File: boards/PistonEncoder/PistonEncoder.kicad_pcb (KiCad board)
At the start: 2 copper layers, 26 parts, among them J1 ISP, J2 PedalExt, J3 LED_Pwr, J4 LEDs1, J5 LEDs2, J6 Pistons1, J7 Pistons2, J8 BoardCon, U1 ATmega48-20P, U2 ULN2803A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

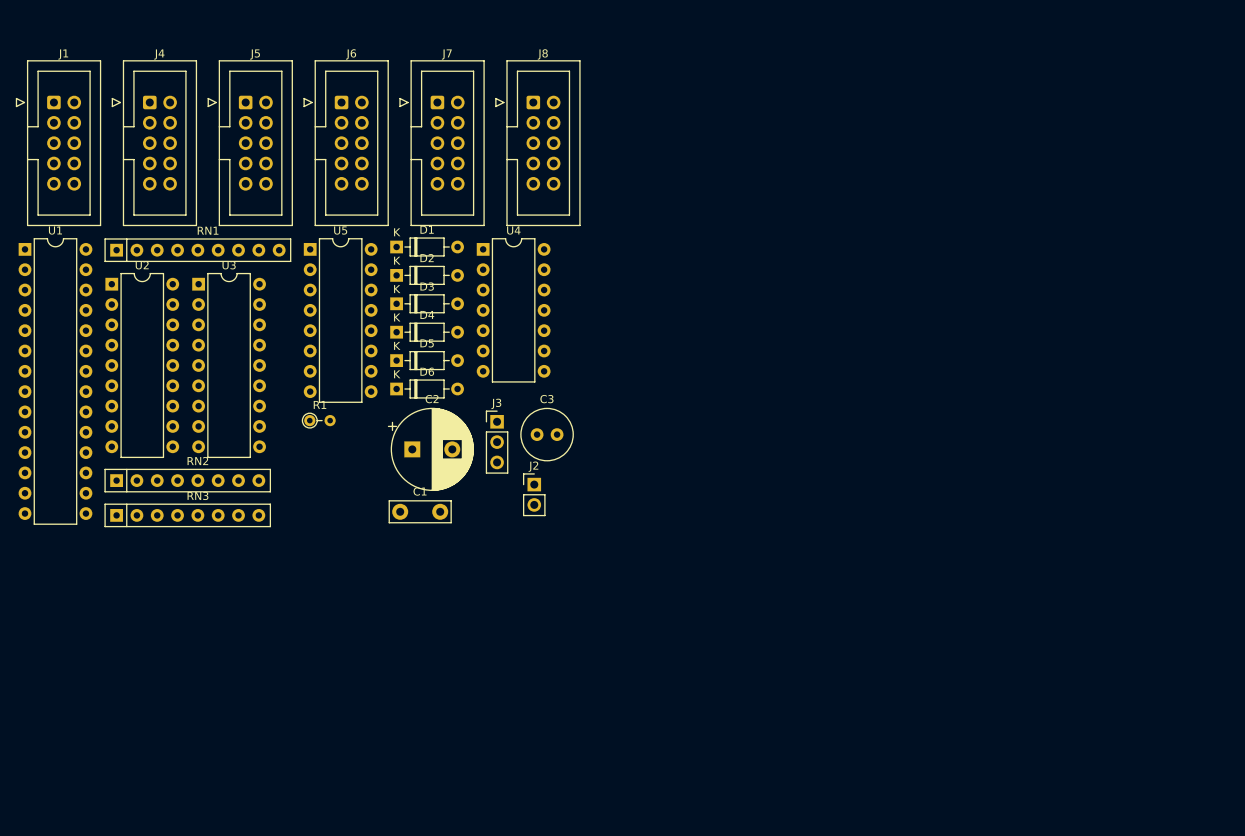
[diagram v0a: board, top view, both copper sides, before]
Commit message: PCB layout for keyboard scanner and piston encoder
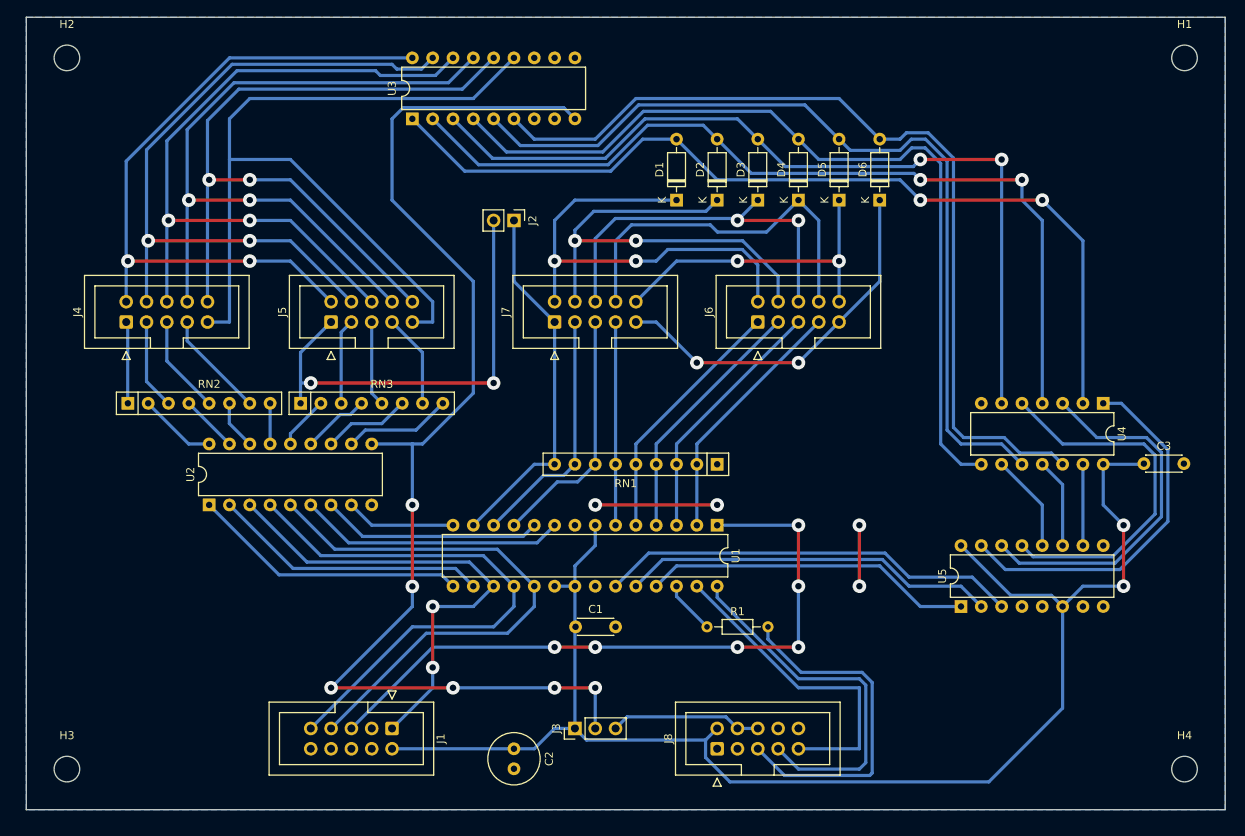
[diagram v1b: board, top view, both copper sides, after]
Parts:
- added H1: MountingHole, MountingHole:MountingHole_3.2mm_M3, F.Cu at (210.8, 50.8)
- added H2: MountingHole, MountingHole:MountingHole_3.2mm_M3, F.Cu at (71.1, 50.8)
- added H3: MountingHole, MountingHole:MountingHole_3.2mm_M3, F.Cu at (71.1, 139.7)
- added H4: MountingHole, MountingHole:MountingHole_3.2mm_M3, F.Cu at (210.8, 139.7)
- C1: value 100nF -> C; footprint Capacitor_THT:C_Disc_D7.5mm_W2.5mm_P5.00mm -> Capacitor_THT:C_Disc_D4.3mm_W1.9mm_P5.00mm
- C2: footprint Capacitor_THT:CP_Radial_D10.0mm_P5.00mm -> Capacitor_THT:C_Radial_D6.3mm_H7.0mm_P2.50mm
- C3: value 100nF -> C; footprint Capacitor_THT:C_Radial_D6.3mm_H11.0mm_P2.50mm -> Capacitor_THT:C_Disc_D4.3mm_W1.9mm_P5.00mm
- J2: value PedalExt -> Ext
- J3: value LED_Pwr -> PWR
- J4: value LEDs1 -> LED1
- J5: value LEDs2 -> LED2
- R1: value 220 -> R; footprint Resistor_THT:R_Axial_DIN0204_L3.6mm_D1.6mm_P2.54mm_Vertical -> Resistor_THT:R_Axial_DIN0204_L3.6mm_D1.6mm_P7.62mm_Horizontal
- RN2, RN3: value R_Pack04 -> R_Pack04_SIP_Split
- moved U1 93.1 mm to (152.4, 109.2), turned to -90 degrees
- moved U5 92.8 mm to (182.9, 119.4), turned to 90 degrees
- moved J1 88.9 mm to (111.8, 134.6), turned to -90 degrees
- moved J8 84.0 mm to (152.4, 137.2), turned to 90 degrees
- moved U4 79.9 mm to (200.7, 94.0), turned to -90 degrees
- moved RN1 79.7 mm to (152.4, 101.6), turned to 180 degrees
- moved C3 75.9 mm to (205.7, 101.5)
- moved D6 64.8 mm to (172.7, 68.6), turned to 90 degrees
- moved D5 58.8 mm to (167.6, 68.6), turned to 90 degrees
- moved J6 58.8 mm to (157.5, 83.8), turned to 90 degrees
- moved R1 55.9 mm to (151.1, 121.9)
- moved D4 52.9 mm to (162.6, 68.6), turned to 90 degrees
- moved D3 47.0 mm to (157.5, 68.6), turned to 90 degrees
- moved D2 41.2 mm to (152.4, 68.6), turned to 90 degrees
- moved J3 39.5 mm to (134.6, 134.6), turned to 90 degrees
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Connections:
- J2 pad 1: Net-(J2-Pin_1) -> P8
- J6 pad 1: Net-(J6-Pin_1) -> P4
- J6 pad 3: Net-(J6-Pin_3) -> P3
- J6 pad 5: Net-(J6-Pin_5) -> P2
- J6 pad 7: Net-(J6-Pin_7) -> P1
- J7 pad 1: Net-(J2-Pin_1) -> P8
- J7 pad 3: Net-(J7-Pin_3) -> P7
- J7 pad 5: Net-(J7-Pin_5) -> P6
- J7 pad 7: Net-(J7-Pin_7) -> P5
- RN1 pad 2: Net-(J6-Pin_1) -> P1
- RN1 pad 3: Net-(J6-Pin_3) -> P2
- RN1 pad 4: Net-(J6-Pin_5) -> P3
- RN1 pad 5: Net-(J6-Pin_7) -> P4
- RN1 pad 6: Net-(J2-Pin_1) -> P5
- RN1 pad 7: Net-(J7-Pin_3) -> P6
- RN1 pad 8: Net-(J7-Pin_5) -> P7
- RN1 pad 9: Net-(J7-Pin_7) -> P8
- RN2 pad 1: Net-(J4-Pin_7) -> Net-(J4-Pin_1)
- RN2 pad 2: Net-(J4-Pin_5) -> Net-(RN2A-R1.2)
- RN2 pad 4: Net-(J4-Pin_1) -> Net-(RN2B-R2.2)
- RN2 pad 5: Net-(RN2-R4.2) -> Net-(J4-Pin_5)
- RN2 pad 6: Net-(RN2-R3.2) -> Net-(RN2C-R3.2)
- RN2 pad 7: Net-(RN2-R2.2) -> Net-(J4-Pin_7)
- RN3 pad 1: Net-(J5-Pin_7) -> Net-(J2-Pin_2)
- RN3 pad 2: Net-(J5-Pin_5) -> Net-(RN3A-R1.2)
- RN3 pad 4: Net-(J2-Pin_2) -> Net-(RN3B-R2.2)
- RN3 pad 5: Net-(RN3-R4.2) -> Net-(J5-Pin_5)
- RN3 pad 6: Net-(RN3-R3.2) -> Net-(RN3C-R3.2)
- RN3 pad 7: Net-(RN3-R2.2) -> Net-(J5-Pin_7)
- U1 pad 11: Net-(J7-Pin_3) -> P6
- U1 pad 12: Net-(J7-Pin_5) -> P7
- U1 pad 13: Net-(J7-Pin_7) -> P8
- U1 pad 2: Net-(J6-Pin_1) -> P1
- U1 pad 23: A1 -> A3
- U1 pad 25: A3 -> A1
- U1 pad 3: Net-(J6-Pin_3) -> P2
- U1 pad 4: Net-(J6-Pin_5) -> P3
- U1 pad 5: Net-(J6-Pin_7) -> P4
- U1 pad 6: Net-(J2-Pin_1) -> P5
- U2 pad 1: Net-(U1-PB0) -> Net-(U1-PB1)
- U2 pad 12: Net-(RN3-R2.2) -> Net-(RN3C-R3.2)
- U2 pad 13: Net-(RN3-R3.2) -> Net-(RN3B-R2.2)
- U2 pad 14: Net-(RN3-R4.2) -> Net-(RN3A-R1.2)
- U2 pad 16: Net-(RN2-R2.2) -> Net-(RN2C-R3.2)
- U2 pad 17: Net-(RN2-R3.2) -> Net-(RN2B-R2.2)
- U2 pad 18: Net-(RN2-R4.2) -> Net-(RN2A-R1.2)
- U2 pad 2: Net-(U1-PB1) -> Net-(U1-PB2)
- U2 pad 3: Net-(U1-PB2) -> MOSI
- U2 pad 4: MOSI -> MISO
- U2 pad 5: MISO -> SCK
- U2 pad 6: SCK -> Net-(U1-XTAL1/PB6)
- U2 pad 7: Net-(U1-XTAL1/PB6) -> Net-(U1-XTAL2/PB7)
- U2 pad 8: Net-(U1-XTAL2/PB7) -> Net-(U1-PB0)
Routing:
- net +5V: track 0.00 -> 182.3 mm, vias 0 -> 2
- net Net-(J3-Pin_2): track 0.00 -> 150.6 mm, vias 0 -> 6
- net L1: track 0.00 -> 113.8 mm, vias 0 -> 2
- net L6: track 0.00 -> 111.1 mm
- net L2: track 0.00 -> 109.9 mm, vias 0 -> 2
- net L5: track 0.00 -> 109.0 mm
- net L4: track 0.00 -> 107.3 mm
- net L3: track 0.00 -> 106.0 mm, vias 0 -> 2
- net Net-(J4-Pin_9): track 0.00 -> 104.7 mm
- net Net-(J4-Pin_10): track 0.00 -> 93.6 mm, vias 0 -> 2
- net Net-(J4-Pin_8): track 0.00 -> 91.9 mm, vias 0 -> 2
- net Net-(J4-Pin_6): track 0.00 -> 90.5 mm, vias 0 -> 2
- net Net-(J4-Pin_4): track 0.00 -> 88.8 mm, vias 0 -> 2
- net Net-(J4-Pin_2): track 0.00 -> 86.4 mm, vias 0 -> 2
- net Reset: track 0.00 -> 85.5 mm, vias 0 -> 6
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- added copper zone on B.Cu, net GND
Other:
- board outline added: 149.9 x 99.1 mm

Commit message: Updated to KiCAD 8, fixed optocouplers for MIDI and added powersupplies
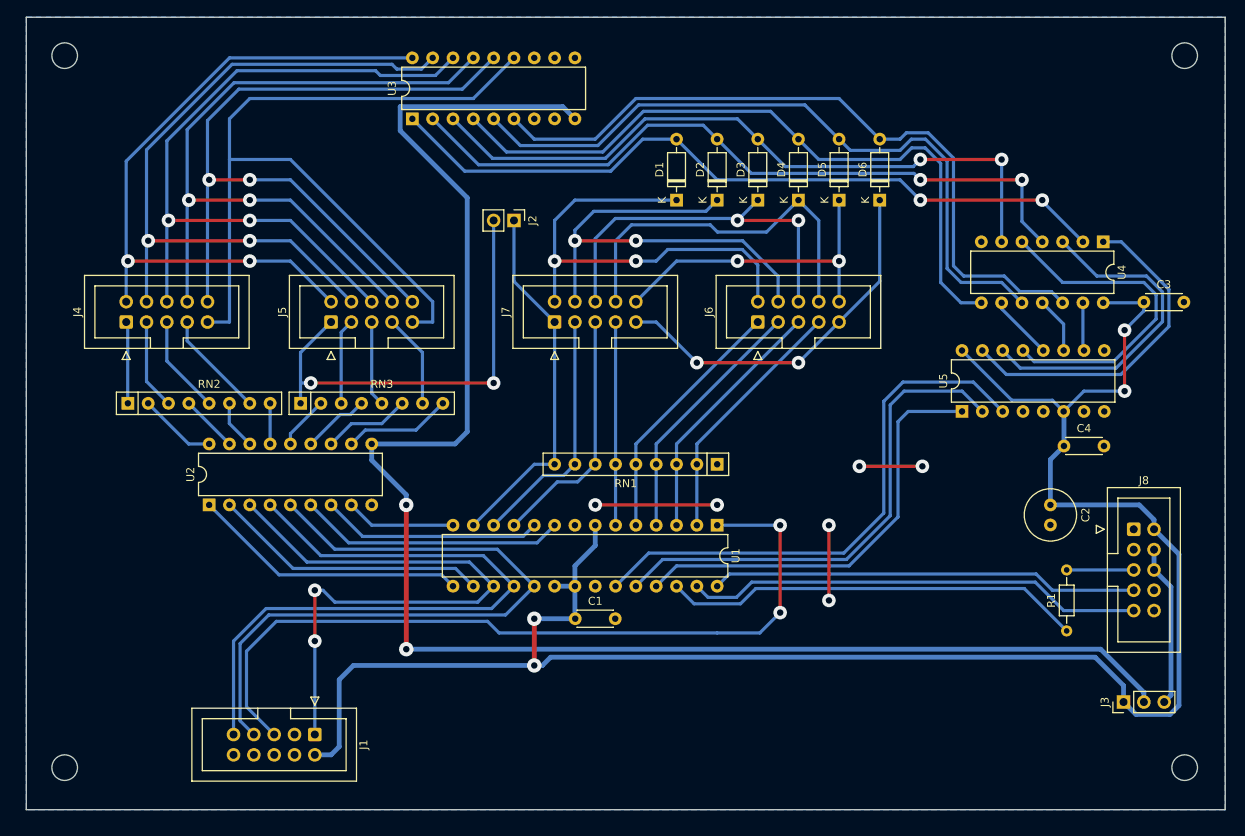
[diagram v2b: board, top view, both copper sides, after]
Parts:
- added C4: 100nF, Capacitor_THT:C_Disc_D4.3mm_W1.9mm_P5.00mm, F.Cu at (195.8, 99.3)
- C1, C3: value C -> 100nF
- C2: value C_Polarized -> 10uF
- moved C2 73.7 mm to (194.1, 106.7)
- moved J3 68.7 mm to (203.2, 131.3)
- moved J8 58.9 mm to (204.5, 109.7), turned to 0 degrees
- moved R1 45.0 mm to (196.1, 122.4), turned to 90 degrees
- moved U5 24.4 mm to (183.0, 95.0)
- moved C3 20.2 mm to (205.7, 81.3)
- moved U4 20.2 mm to (200.7, 73.8)
- moved J1 9.68 mm to (102.1, 135.4)
- moved C1 1.02 mm to (134.7, 120.9)
- moved H2 0.40 mm to (70.8, 50.5)
- moved H3 0.33 mm to (70.8, 139.5)
- moved H1 0.28 mm to (210.8, 50.5)
- moved H4 0.18 mm to (210.8, 139.5)
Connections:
- net Net-(J3-Pin_2) renamed /LED_PWR
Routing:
- net +5V: track 182.3 -> 241.3 mm, vias 2 -> 4
- net /LED_PWR: track 150.6 -> 202.2 mm, vias 6 -> 2
- net Interrupt: track 6.66 -> 52.7 mm
- net Net-(J8-Pin_5): track 43.9 -> 8.38 mm
- net L5: track 109.0 -> 88.8 mm
- net L4: track 107.3 -> 87.1 mm
- net L3: track 106.0 -> 85.8 mm
- net L1: track 113.8 -> 93.6 mm
- net L6: track 111.1 -> 90.9 mm
- net L2: track 109.9 -> 89.7 mm
- net SCK: track 68.9 -> 86.5 mm
- net SDA: track 40.8 -> 57.5 mm
- net A3: track 52.7 -> 68.7 mm
- net MOSI: track 60.7 -> 76.5 mm
- net A2: track 47.0 -> 62.6 mm
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
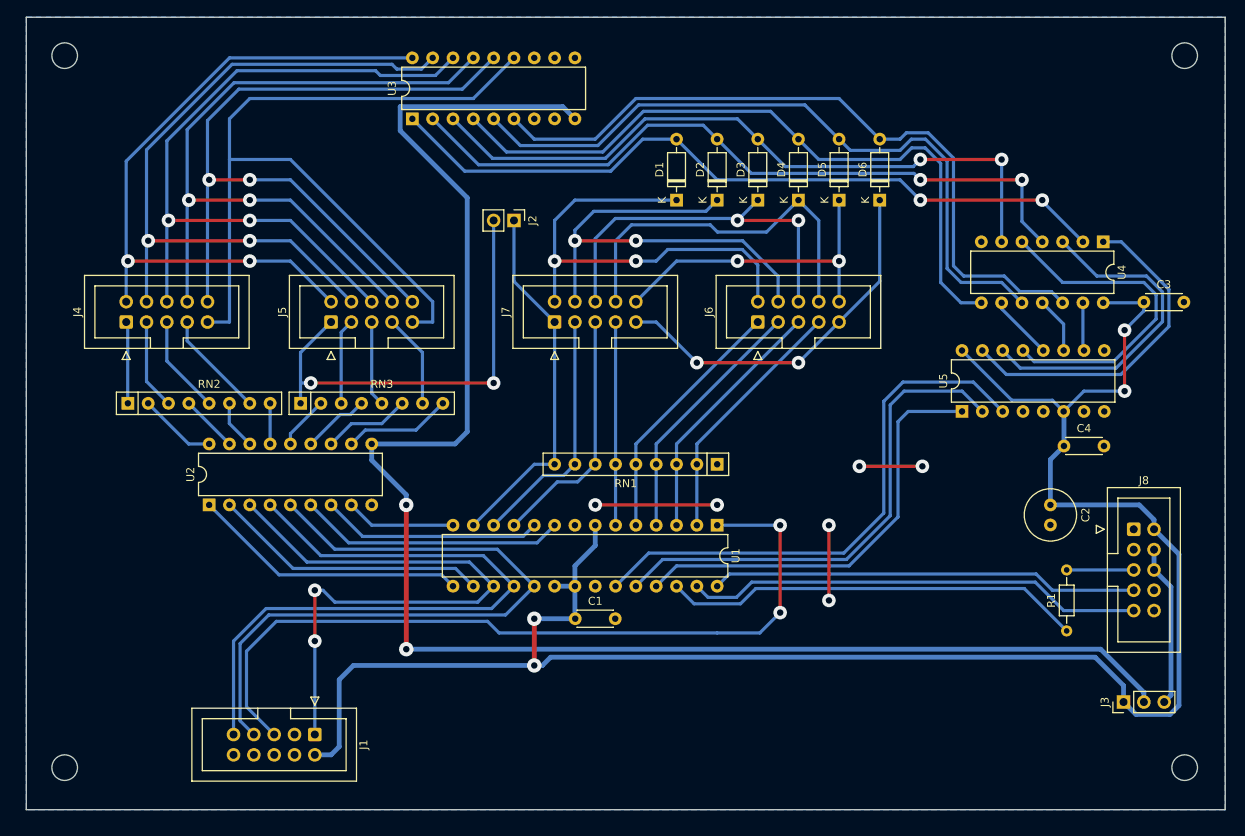
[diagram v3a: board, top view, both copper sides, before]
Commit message: Cleanup of PCB sizes and mounthole positions. Moved MIDI connectors to separate board.
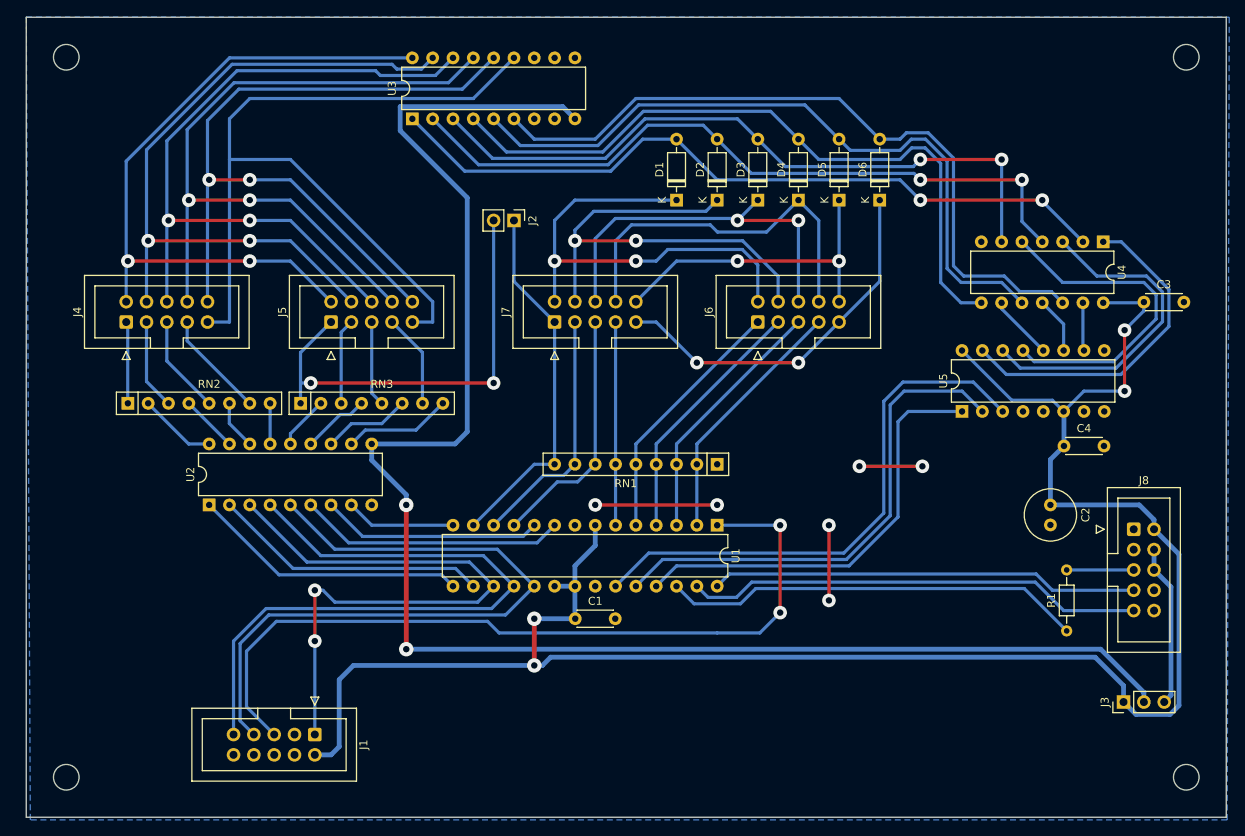
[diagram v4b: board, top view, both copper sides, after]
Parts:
- moved H3 1.22 mm to (71.0, 140.7)
- moved H4 1.22 mm to (211.0, 140.7)
- moved H2 0.28 mm to (71.0, 50.7)
- moved H1 0.28 mm to (211.0, 50.7)
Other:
- board size 149.9 x 99.1 mm -> 150 x 100 mm
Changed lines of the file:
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@@
 		(pad_to_mask_clearance 0)
 		(allow_soldermask_bridges_in_footprints no)
+		(aux_axis_origin 66.04 45.72)
 		(pcbplotparams
 			(layerselection 0x00010fc_ffffffff)
@@
 	(footprint "MountingHole:MountingHole_3.2mm_M3"
 		(layer "F.Cu")
-		(at 210.84 50.52)
+		(at 211.04 50.72)
 		(descr "Mounting Hole 3.2mm, no annular, M3")
 		(tags "mounting hole 3.2mm no annular m3")
@@
 	(footprint "MountingHole:MountingHole_3.2mm_M3"
 		(layer "F.Cu")
-		(at 210.84 139.52)
+		(at 211.04 140.72)
 		(descr "Mounting Hole 3.2mm, no annular, M3")
 		(tags "mounting hole 3.2mm no annular m3")
@@
 	(footprint "MountingHole:MountingHole_3.2mm_M3"
 		(layer "F.Cu")
-		(at 70.84 50.52)
+		(at 71.04 50.72)
 		(descr "Mounting Hole 3.2mm, no annular, M3")
 		(tags "mounting hole 3.2mm no annular m3")
@@
 	(footprint "MountingHole:MountingHole_3.2mm_M3"
 		(layer "F.Cu")
-		(at 70.84 139.52)
+		(at 71.04 140.72)
 		(descr "Mounting Hole 3.2mm, no annular, M3")
 		(tags "mounting hole 3.2mm no annular m3")
@@
 	(gr_rect
 		(start 66.04 45.72)
-		(end 215.9 144.78)
+		(end 216.04 145.72)
 		(stroke
 			(width 0.1)
@@
 		(layer "Cmts.User")
 		(pts
-			(xy 66.04 45.72) (xy 70.84 50.52)
+			(xy 71.04 50.72) (xy 66.04 45.72)
 		)
-		(height -5.08)
+		(height -10.08)
 		(orientation 0)
-		(gr_text "4,8000 mm"
-			(at 68.44 39.49 0)
+		(gr_text "5,0000 mm"
+			(at 68.54 39.49 0)
 			(layer "Cmts.User")
 			(effects
@@
 		(layer "Cmts.User")
 		(pts
-			(xy 70.84 50.52) (xy 66.04 45.72)
+			(xy 71.04 50.72) (xy 71.04 140.72)
 		)
-		(height -8.864)
+		(height -11.604)
 		(orientation 1)
-		(gr_text "4,8000 mm"
-			(at 60.826 48.12 90)
+		(gr_text "90,0000 mm"
+			(at 58.286 95.72 90)
 			(layer "Cmts.User")
 			(effects
@@
 		(layer "Cmts.User")
 		(pts
-			(xy 215.9 45.72) (xy 66.04 45.72)
+			(xy 66.04 45.72) (xy 216.04 45.72)
 		)
-		(height -9.652)
+		(height -10.414)
 		(orientation 0)
-		(gr_text "149,8600 mm"
-			(at 140.97 34.918 0)
+		(gr_text "150,0000 mm"
+			(at 141.04 34.156 0)
 			(layer "Cmts.User")
 			(effects
@@
 		(layer "Cmts.User")
 		(pts
-			(xy 70.84 50.52) (xy 70.84 139.52)
+			(xy 71.04 140.72) (xy 211.04 140.72)
 		)
-		(height -8.864)
+		(height 11.934)
+		(orientation 0)
+		(gr_text "140,0000 mm"
+			(at 141.04 151.504 0)
+			(layer "Cmts.User")
+			(effects
+				(font
+					(size 1 1)
+					(thickness 0.15)
+				)
+			)
+		)
+		(format
+			(prefix "")
+			(suffix "")
+			(units 3)
+			(units_format 1)
+			(precision 4)
+		)
+		(style
+			(thickness 0.1)
+			(arrow_length 1.27)
+			(text_position_mode 0)
+			(extension_height 0.58642)
+			(extension_offset 0.5) keep_text_aligned)
+	)
+	(dimension
+		(type orthogonal)
+		(layer "Cmts.User")
+		(pts
+			(xy 66.04 45.72) (xy 71.04 50.72)
+		)
+		(height -6.604)
 		(orientation 1)
-		(gr_text "89,0000 mm"
-			(at 60.826 95.02 90)
+		(gr_text "5,0000 mm"
+			(at 58.286 48.22 90)
 			(layer "Cmts.User")
 			(effects
@@
 		(layer "Cmts.User")
 		(pts
-			(xy 215.9 45.72) (xy 215.9 144.78)
+			(xy 216.04 45.72) (xy 216.04 145.72)
 		)
-		(height 10.922)
+		(height 11.29)
 		(orientation 1)
-		(gr_text "99,0600 mm"
-			(at 225.022 95.25 90)
+		(gr_text "100,0000 mm"
+			(at 226.18 95.72 90)
 			(layer "Cmts.User")
 			(effects
 				(font
-					(size 1.5 1.5)
-					(thickness 0.3)
+					(size 1 1)
+					(thickness 0.15)
 				)
 			)
@@
 		)
 		(style
-			(thickness 0.2)
+			(thickness 0.1)
 			(arrow_length 1.27)
 			(text_position_mode 0)
@@
 		(polygon
 			(pts
-				(xy 66.04 45.72) (xy 215.9 45.72) (xy 215.9 144.78) (xy 66.04 144.78)
+				(xy 66.04 45.72) (xy 216.408 45.72) (xy 216.154 146.05) (xy 66.548 146.05)
 			)
 		)

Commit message: Fixed interrupt line to use open collector, added pullups to I2C lines
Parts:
- added Q1: BC547, Package_TO_SOT_THT:TO-92L_Inline_Wide, F.Cu at (183.1, 113.4)
- R1: value R -> 4k7
- moved R1 19.2 mm to (177.3, 118.6)
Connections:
- R1 pad 2: Net-(J8-Pin_5) -> Net-(Q1-B)
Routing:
- net Interrupt: track 52.7 -> 32.3 mm
- net Net-(J8-Pin_5): track 8.38 -> 22.0 mm
- net Net-(Q1-B): track 0.00 -> 5.61 mm
- net MOSI: track 76.5 -> 76.0 mm
